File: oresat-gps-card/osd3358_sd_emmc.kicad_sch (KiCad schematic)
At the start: 66 parts, among them J4 DM3BT-DSF-PEJS, U1 OSD3358-512M-BSM, U24 25AAXX, U8 TCAN330, U9 EMMC+RESET+5.1-COMPATIBLE-BA

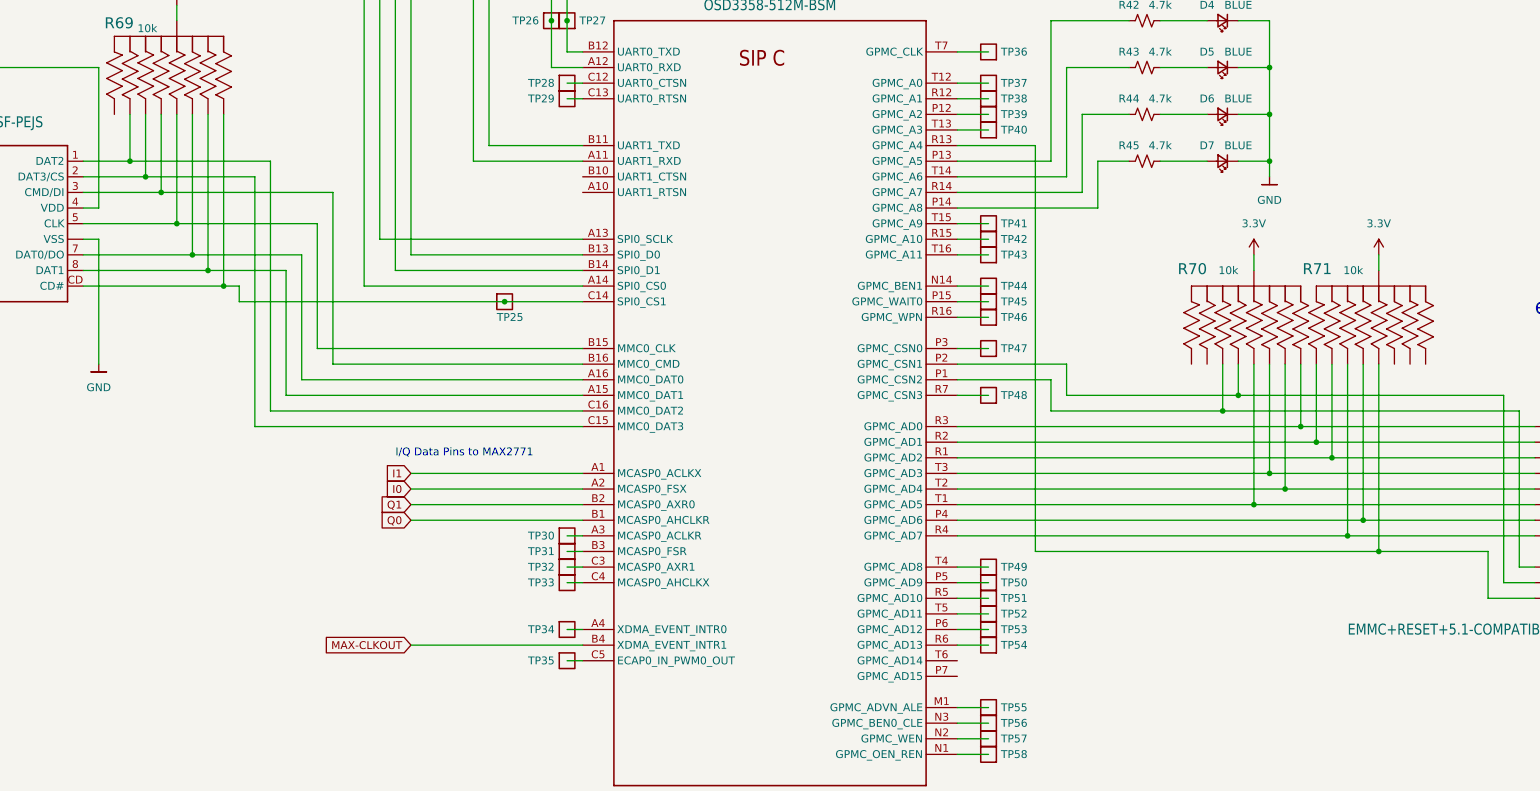
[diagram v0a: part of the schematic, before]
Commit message: GPS card design review changes and issue fixes
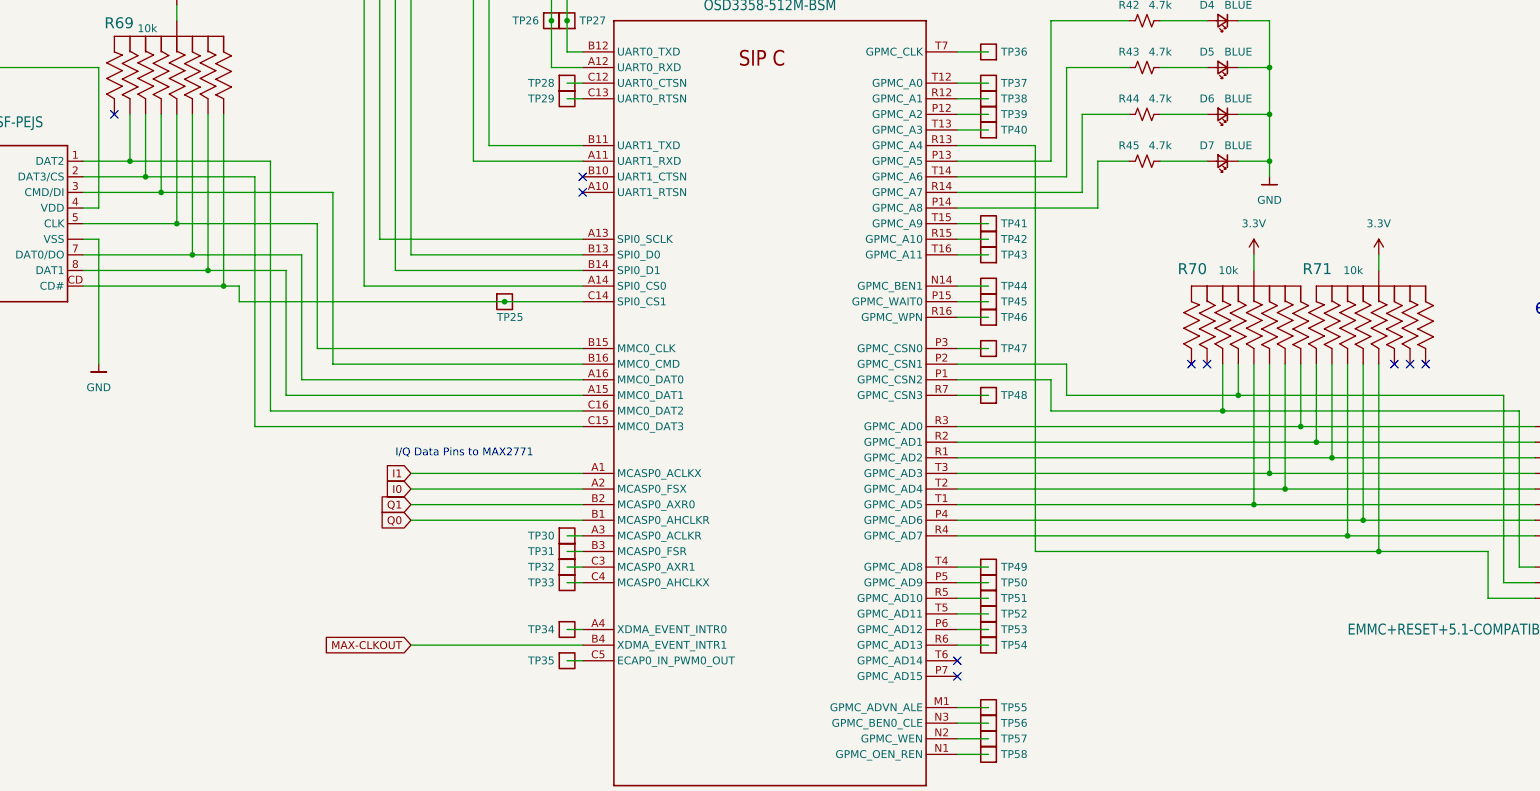
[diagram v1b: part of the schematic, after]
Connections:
- no-connect marks 0 -> 10
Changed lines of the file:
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@@
   (junction (at 330.2 196.85) (diameter 0) (color 0 0 0 0)
   )
+  (no_connect (at 86.36 111.76))
+  (no_connect (at 261.62 152.4))
+  (no_connect (at 264.16 152.4))
+  (no_connect (at 294.64 152.4))
+  (no_connect (at 297.18 152.4))
+  (no_connect (at 299.72 152.4))
+  (no_connect (at 223.52 203.2))
+  (no_connect (at 223.52 200.66))
+  (no_connect (at 162.56 124.46))
+  (no_connect (at 162.56 121.92))
   (wire (pts (xy 269.24 111.76) (xy 274.32 111.76))
     (stroke (width 0) (type default) (color 0 0 0 0))
